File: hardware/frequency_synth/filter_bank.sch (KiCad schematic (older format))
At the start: 33 parts

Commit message: finished initial schematic of synth module
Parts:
- gave numbers to parts that had none: 33

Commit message: reducing component values across module, synth schematic cleanups
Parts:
- C41, C47, C48, C49, C50, C55, C56, C57, C61: value C_Small -> 100 pF
- C42, C60: value C_Small -> 100 nF
- C43, C44, C45, C46, C51, C52, C53, C54: value C_Small -> 30 pF
- C58: value C_Small -> 10 uF; footprint Capacitors_SMD:C_0805 -> Capacitors_SMD:C_0603
- C59: value C_Small -> .1 uF

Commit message: started on component placement
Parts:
- C319: renamed from C59; value .1 uF -> 100 nF
- renumbered C41 to C301, C42 to C302, C43 to C303, C44 to C304, C45 to C305, C46 to C306, C47 to C307, C48 to C308, C49 to C309, C50 to C310, C51 to C311, C52 to C312, C53 to C313, C54 to C314, C55 to C315, C56 to C316, C57 to C317, C58 to C318, C60 to C320, C61 to C321, FI1 to FI301, FI2 to FI302, FI3 to FI303, FI4 to FI304, FI5 to FI305, FI6 to FI306, FI7 to FI307, U6 to U301, U7 to U302, U8 to U303, U9 to U304, U10 to U305

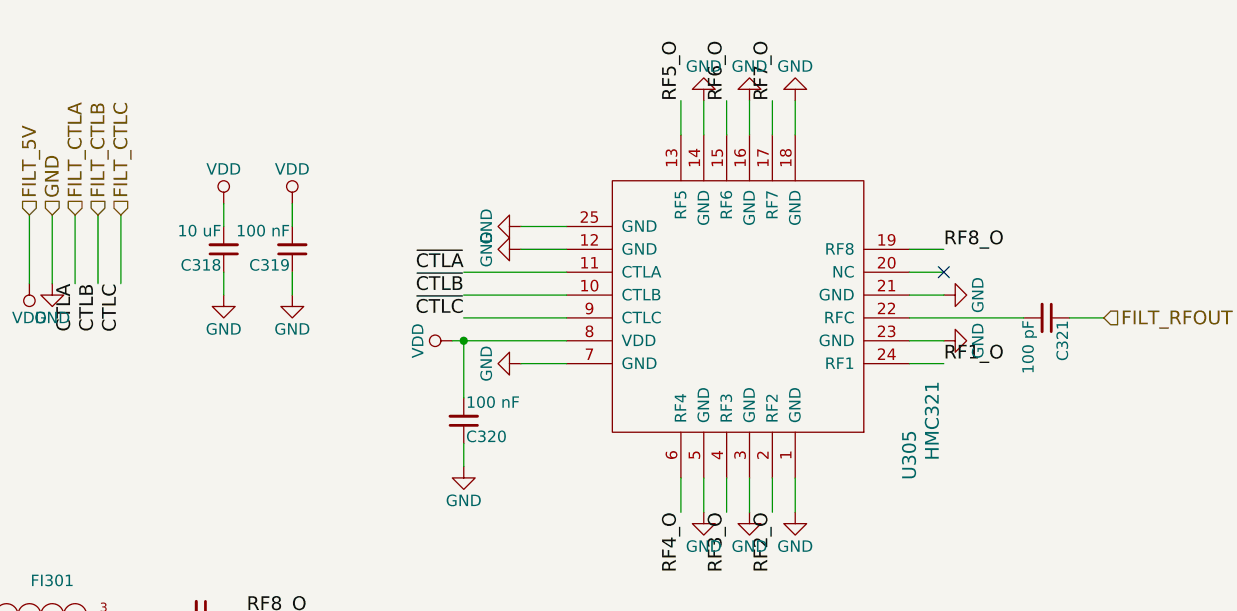
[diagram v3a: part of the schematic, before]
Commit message: synth - initial component placement layout on everybody but lmx2592
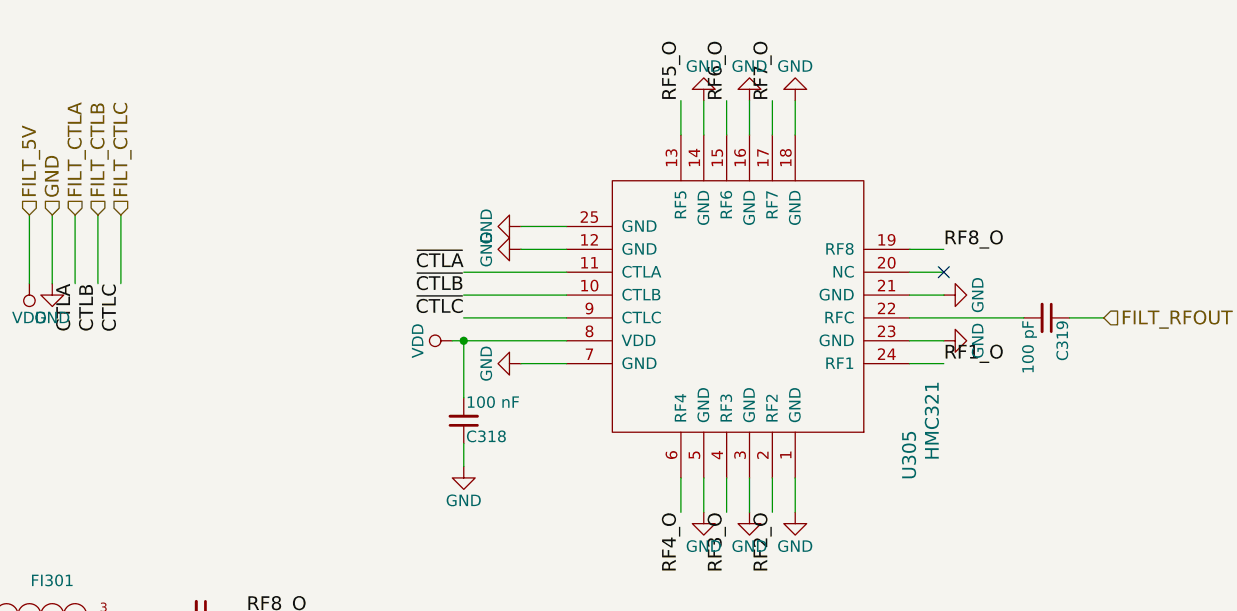
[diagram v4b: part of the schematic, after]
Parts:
- removed C318: 10 uF, Capacitors_SMD:C_0603, symbol C_Small
- removed C319: 100 nF, Capacitors_SMD:C_0402, symbol C_Small
- renumbered C320 to C318, C321 to C319
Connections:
- wire segments 114 -> 110
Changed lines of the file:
@@
 $EndComp
 $Comp
-L C_Small C321
+L C_Small C319
 U 1 1 572ADD77
 P 9950 1750
-F 0 "C321" H 9960 1820 50  0000 L CNN
+F 0 "C319" H 9960 1820 50  0000 L CNN
 F 1 "100 pF" H 9960 1670 50  0000 L CNN
 F 2 "Capacitors_SMD:C_0402" H 9950 1750 50  0001 C CNN
@@
 	7850 1750 7400 1750
 $Comp
-L C_Small C320
+L C_Small C318
 U 1 1 572ADD84
 P 7400 2200
-F 0 "C320" H 7410 2270 50  0000 L CNN
+F 0 "C318" H 7410 2270 50  0000 L CNN
 F 1 "100 nF" H 7410 2120 50  0000 L CNN
 F 2 "Capacitors_SMD:C_0402" H 7400 2200 50  0001 C CNN
@@
 Wire Wire Line
 	5600 1300 5600 1600
-$Comp
-L C_Small C319
-U 1 1 572ADD89
-P 6650 1450
-F 0 "C319" H 6660 1520 50  0000 L CNN
-F 1 "100 nF" H 6660 1370 50  0000 L CNN
-F 2 "Capacitors_SMD:C_0402" H 6650 1450 50  0001 C CNN
-F 3 "" H 6650 1450 50  0000 C CNN
-	1    6650 1450
-	-1   0    0    1
-$EndComp
-$Comp
-L VDD #PWR0113
-U 1 1 572ADD8A
-P 6650 1250
-F 0 "#PWR0113" H 6650 1100 50  0001 C CNN
-F 1 "VDD" H 6650 1400 50  0000 C CNN
-F 2 "" H 6650 1250 50  0000 C CNN
-F 3 "" H 6650 1250 50  0000 C CNN
-	1    6650 1250
-	1    0    0    -1
-$EndComp
-Wire Wire Line
-	6650 1250 6650 1350
-$Comp
-L GND #PWR0114
-U 1 1 572ADD8B
-P 6650 1650
-F 0 "#PWR0114" H 6650 1400 50  0001 C CNN
-F 1 "GND" H 6650 1500 50  0000 C CNN
-F 2 "" H 6650 1650 50  0000 C CNN
-F 3 "" H 6650 1650 50  0000 C CNN
-	1    6650 1650
-	-1   0    0    -1
-$EndComp
-Wire Wire Line
-	6650 1650 6650 1550
-$Comp
-L C_Small C318
-U 1 1 572ADD8C
-P 6350 1450
-F 0 "C318" H 6360 1520 50  0000 L CNN
-F 1 "10 uF" H 6360 1370 50  0000 L CNN
-F 2 "Capacitors_SMD:C_0603" H 6350 1450 50  0001 C CNN
-F 3 "" H 6350 1450 50  0000 C CNN
-	1    6350 1450
-	-1   0    0    1
-$EndComp
-$Comp
-L VDD #PWR0115
-U 1 1 572ADD8D
-P 6350 1250
-F 0 "#PWR0115" H 6350 1100 50  0001 C CNN
-F 1 "VDD" H 6350 1400 50  0000 C CNN
-F 2 "" H 6350 1250 50  0000 C CNN
-F 3 "" H 6350 1250 50  0000 C CNN
-	1    6350 1250
-	1    0    0    -1
-$EndComp
-Wire Wire Line
-	6350 1250 6350 1350
-$Comp
-L GND #PWR0116
-U 1 1 572ADD8E
-P 6350 1650
-F 0 "#PWR0116" H 6350 1400 50  0001 C CNN
-F 1 "GND" H 6350 1500 50  0000 C CNN
-F 2 "" H 6350 1650 50  0000 C CNN
-F 3 "" H 6350 1650 50  0000 C CNN
-	1    6350 1650
-	-1   0    0    -1
-$EndComp
-Wire Wire Line
-	6350 1650 6350 1550
 $Comp
 L 74xx1G14 U303
@@
 	1200 6950 1450 6950
 $Comp
-L GND #PWR0117
+L GND #PWR0113
 U 1 1 572ADD91
 P 1900 7550
-F 0 "#PWR0117" H 1900 7300 50  0001 C CNN
+F 0 "#PWR0113" H 1900 7300 50  0001 C CNN
 F 1 "GND" H 1900 7400 50  0000 C CNN
 F 2 "" H 1900 7550 50  0000 C CNN
@@
 	1900 7550 1900 7450
 $Comp
-L VDD #PWR0118
+L VDD #PWR0114
 U 1 1 572ADD92
 P 1900 6350
-F 0 "#PWR0118" H 1900 6200 50  0001 C CNN
+F 0 "#PWR0114" H 1900 6200 50  0001 C CNN
 F 1 "VDD" H 1900 6500 50  0000 C CNN
 F 2 "" H 1900 6350 50  0000 C CNN
@@
 	1200 5200 1450 5200
 $Comp
-L GND #PWR0119
+L GND #PWR0115
 U 1 1 572ADD94
 P 1900 5800
-F 0 "#PWR0119" H 1900 5550 50  0001 C CNN
+F 0 "#PWR0115" H 1900 5550 50  0001 C CNN
 F 1 "GND" H 1900 5650 50  0000 C CNN
 F 2 "" H 1900 5800 50  0000 C CNN
@@
 	1900 5800 1900 5700
 $Comp
-L VDD #PWR0120
+L VDD #PWR0116
 U 1 1 572ADD95
 P 1900 4600
-F 0 "#PWR0120" H 1900 4450 50  0001 C CNN
+F 0 "#PWR0116" H 1900 4450 50  0001 C CNN
 F 1 "VDD" H 1900 4750 50  0000 C CNN
 F 2 "" H 1900 4600 50  0000 C CNN
@@
 	1200 3600 1450 3600
 $Comp
-L GND #PWR0121
+L GND #PWR0117
 U 1 1 572ADD97
 P 1900 4200
-F 0 "#PWR0121" H 1900 3950 50  0001 C CNN
+F 0 "#PWR0117" H 1900 3950 50  0001 C CNN
 F 1 "GND" H 1900 4050 50  0000 C CNN
 F 2 "" H 1900 4200 50  0000 C CNN
@@
 	1900 4200 1900 4100
 $Comp
-L VDD #PWR0122
+L VDD #PWR0118
 U 1 1 572ADD98
 P 1900 3000
-F 0 "#PWR0122" H 1900 2850 50  0001 C CNN
+F 0 "#PWR0118" H 1900 2850 50  0001 C CNN
 F 1 "VDD" H 1900 3150 50  0000 C CNN
 F 2 "" H 1900 3000 50  0000 C CNN
@@
 FILT_CTLC
 $Comp
-L GND #PWR0123
+L GND #PWR0119
 U 1 1 572ADD88
 P 5600 1600
-F 0 "#PWR0123" H 5600 1350 50  0001 C CNN
+F 0 "#PWR0119" H 5600 1350 50  0001 C CNN
 F 1 "GND" H 5600 1450 50  0000 C CNN
 F 2 "" H 5600 1600 50  0000 C CNN

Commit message: work on synth layout - removed filter bank inverters
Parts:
- removed U301, U302, U303: 74xx1G14, TO_SOT_Packages_SMD:SOT-23-5, symbol 74xx1G14
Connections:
- net labels added: FILT_~CTLA, FILT_~CTLB, FILT_~CTLC
- wire segments 110 -> 101
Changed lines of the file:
@@
 Wire Wire Line
 	5600 1300 5600 1600
-$Comp
-L 74xx1G14 U303
-U 1 1 572ADD90
-P 1900 6950
-F 0 "U303" H 1350 7300 60  0000 C CNN
-F 1 "74xx1G14" H 1500 7400 60  0000 C CNN
-F 2 "TO_SOT_Packages_SMD:SOT-23-5" H 1900 6950 60  0001 C CNN
-F 3 "" H 1900 6950 60  0000 C CNN
-	1    1900 6950
-	1    0    0    -1
-$EndComp
-Text Label 1200 3600 2    60   ~ 0
-CTLA
-Text Label 1200 5200 2    60   ~ 0
-CTLB
-Text Label 1200 6950 2    60   ~ 0
-CTLC
-Text Label 2650 3600 0    60   ~ 0
+Text Label 6050 1600 3    60   ~ 0
 ~CTLA
-Text Label 2650 5200 0    60   ~ 0
+Text Label 6150 1600 3    60   ~ 0
 ~CTLB
-Text Label 2650 6950 0    60   ~ 0
+Text Label 6250 1600 3    60   ~ 0
 ~CTLC
 Wire Wire Line
-	2650 6950 2350 6950
+	6250 1600 6250 1300
 Wire Wire Line
-	1200 6950 1450 6950
-$Comp
-L GND #PWR0113
-U 1 1 572ADD91
-P 1900 7550
-F 0 "#PWR0113" H 1900 7300 50  0001 C CNN
-F 1 "GND" H 1900 7400 50  0000 C CNN
-F 2 "" H 1900 7550 50  0000 C CNN
-F 3 "" H 1900 7550 50  0000 C CNN
-	1    1900 7550
-	1    0    0    -1
-$EndComp
+	6150 1600 6150 1300
 Wire Wire Line
-	1900 7550 1900 7450
-$Comp
-L VDD #PWR0114
-U 1 1 572ADD92
-P 1900 6350
-F 0 "#PWR0114" H 1900 6200 50  0001 C CNN
-F 1 "VDD" H 1900 6500 50  0000 C CNN
-F 2 "" H 1900 6350 50  0000 C CNN
-F 3 "" H 1900 6350 50  0000 C CNN
-	1    1900 6350
-	1    0    0    -1
-$EndComp
-Wire Wire Line
-	1900 6350 1900 6450
-$Comp
-L 74xx1G14 U302
-U 1 1 572ADD93
-P 1900 5200
-F 0 "U302" H 1350 5550 60  0000 C CNN
-F 1 "74xx1G14" H 1500 5650 60  0000 C CNN
-F 2 "TO_SOT_Packages_SMD:SOT-23-5" H 1900 5200 60  0001 C CNN
-F 3 "" H 1900 5200 60  0000 C CNN
-	1    1900 5200
-	1    0    0    -1
-$EndComp
-Wire Wire Line
-	2650 5200 2350 5200
-Wire Wire Line
-	1200 5200 1450 5200
-$Comp
-L GND #PWR0115
-U 1 1 572ADD94
-P 1900 5800
-F 0 "#PWR0115" H 1900 5550 50  0001 C CNN
-F 1 "GND" H 1900 5650 50  0000 C CNN
-F 2 "" H 1900 5800 50  0000 C CNN
-F 3 "" H 1900 5800 50  0000 C CNN
-	1    1900 5800
-	1    0    0    -1
-$EndComp
-Wire Wire Line
-	1900 5800 1900 5700
-$Comp
-L VDD #PWR0116
-U 1 1 572ADD95
-P 1900 4600
-F 0 "#PWR0116" H 1900 4450 50  0001 C CNN
-F 1 "VDD" H 1900 4750 50  0000 C CNN
-F 2 "" H 1900 4600 50  0000 C CNN
-F 3 "" H 1900 4600 50  0000 C CNN
-	1    1900 4600
-	1    0    0    -1
-$EndComp
-Wire Wire Line
-	1900 4600 1900 4700
-$Comp
-L 74xx1G14 U301
-U 1 1 572ADD96
-P 1900 3600
-F 0 "U301" H 1350 3950 60  0000 C CNN
-F 1 "74xx1G14" H 1500 4050 60  0000 C CNN
-F 2 "TO_SOT_Packages_SMD:SOT-23-5" H 1900 3600 60  0001 C CNN
-F 3 "" H 1900 3600 60  0000 C CNN
-	1    1900 3600
-	1    0    0    -1
-$EndComp
-Wire Wire Line
-	2650 3600 2350 3600
-Wire Wire Line
-	1200 3600 1450 3600
-$Comp
-L GND #PWR0117
-U 1 1 572ADD97
-P 1900 4200
-F 0 "#PWR0117" H 1900 3950 50  0001 C CNN
-F 1 "GND" H 1900 4050 50  0000 C CNN
-F 2 "" H 1900 4200 50  0000 C CNN
-F 3 "" H 1900 4200 50  0000 C CNN
-	1    1900 4200
-	1    0    0    -1
-$EndComp
-Wire Wire Line
-	1900 4200 1900 4100
-$Comp
-L VDD #PWR0118
-U 1 1 572ADD98
-P 1900 3000
-F 0 "#PWR0118" H 1900 2850 50  0001 C CNN
-F 1 "VDD" H 1900 3150 50  0000 C CNN
-F 2 "" H 1900 3000 50  0000 C CNN
-F 3 "" H 1900 3000 50  0000 C CNN
-	1    1900 3000
-	1    0    0    -1
-$EndComp
-Wire Wire Line
-	1900 3000 1900 3100
+	6050 1600 6050 1300
 Text HLabel 10200 1750 2    60   Input ~ 0
 FILT_RFOUT
@@
 Wire Wire Line
 	5500 1300 5500 1600
+Text HLabel 6050 1300 1    60   Input ~ 0
+FILT_~CTLA
+Text HLabel 6150 1300 1    60   Input ~ 0
+FILT_~CTLB
+Text HLabel 6250 1300 1    60   Input ~ 0
+FILT_~CTLC
 $EndSCHEMATC
